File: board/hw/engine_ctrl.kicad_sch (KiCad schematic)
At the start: 6 parts, among them J3 eng, U5 DRV8220

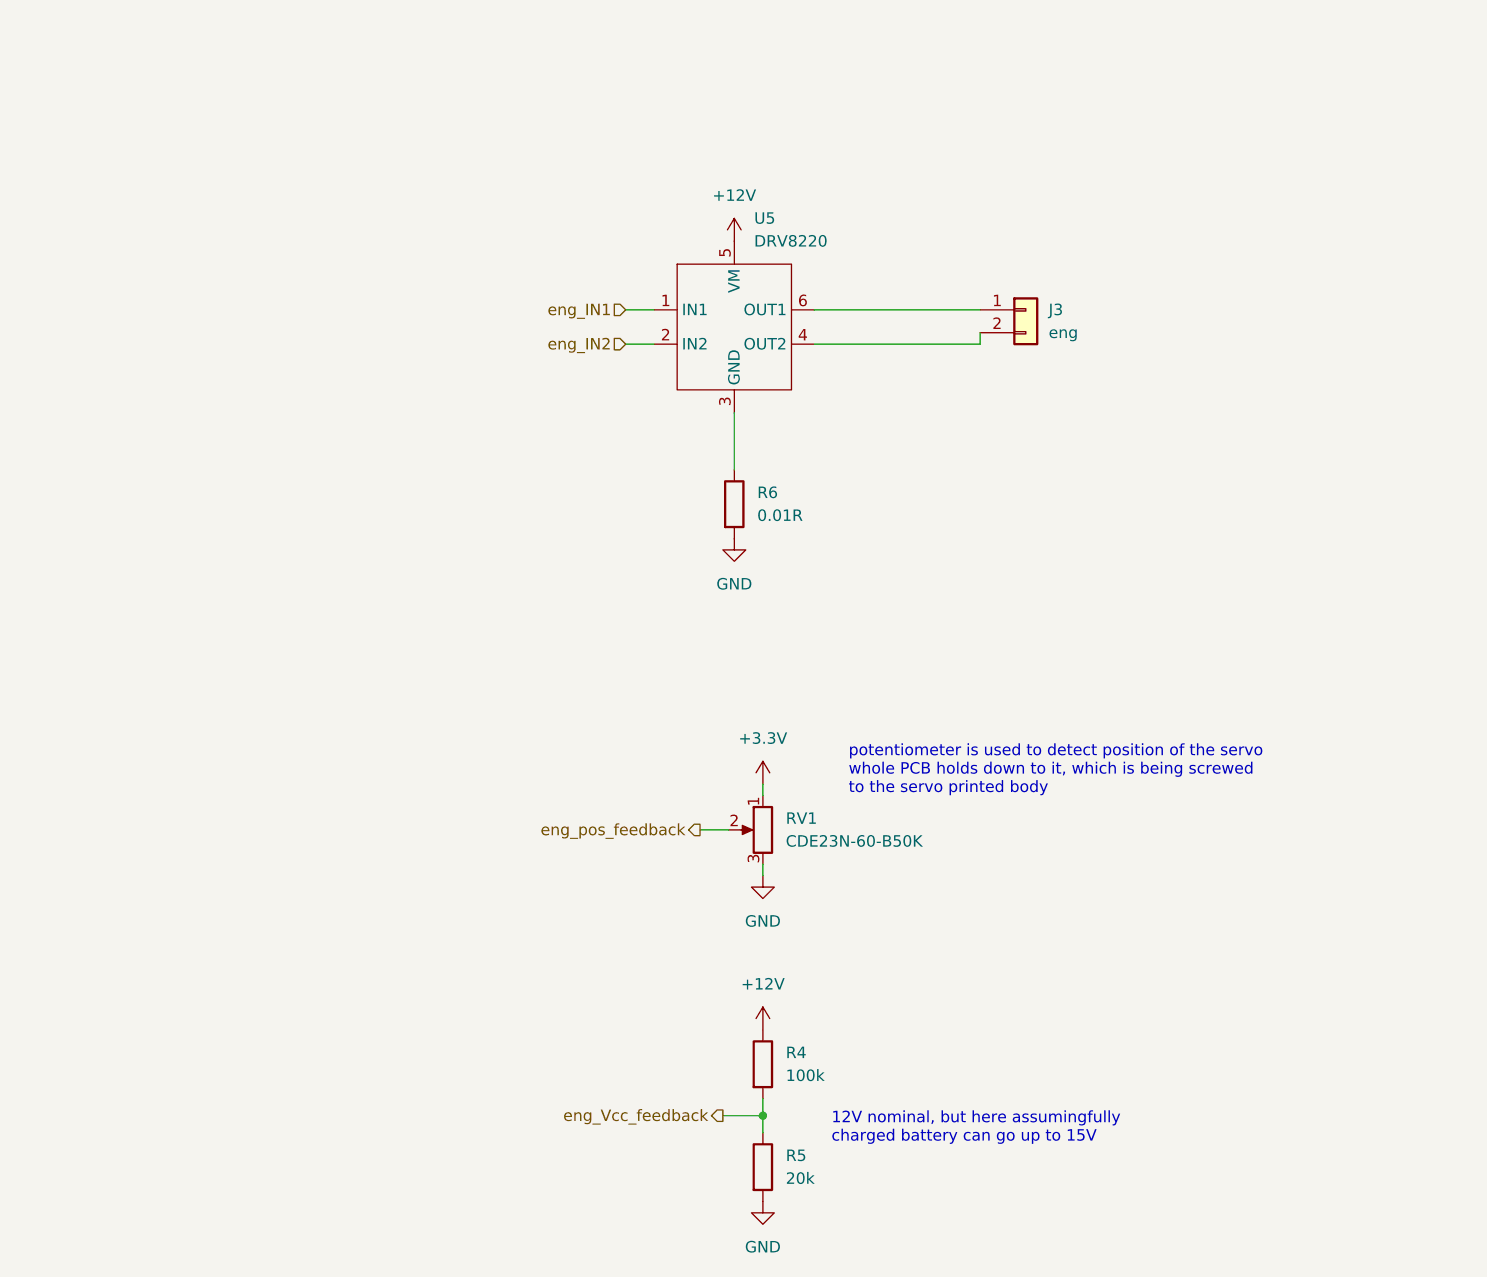
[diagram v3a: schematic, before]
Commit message: added current measuing circuit
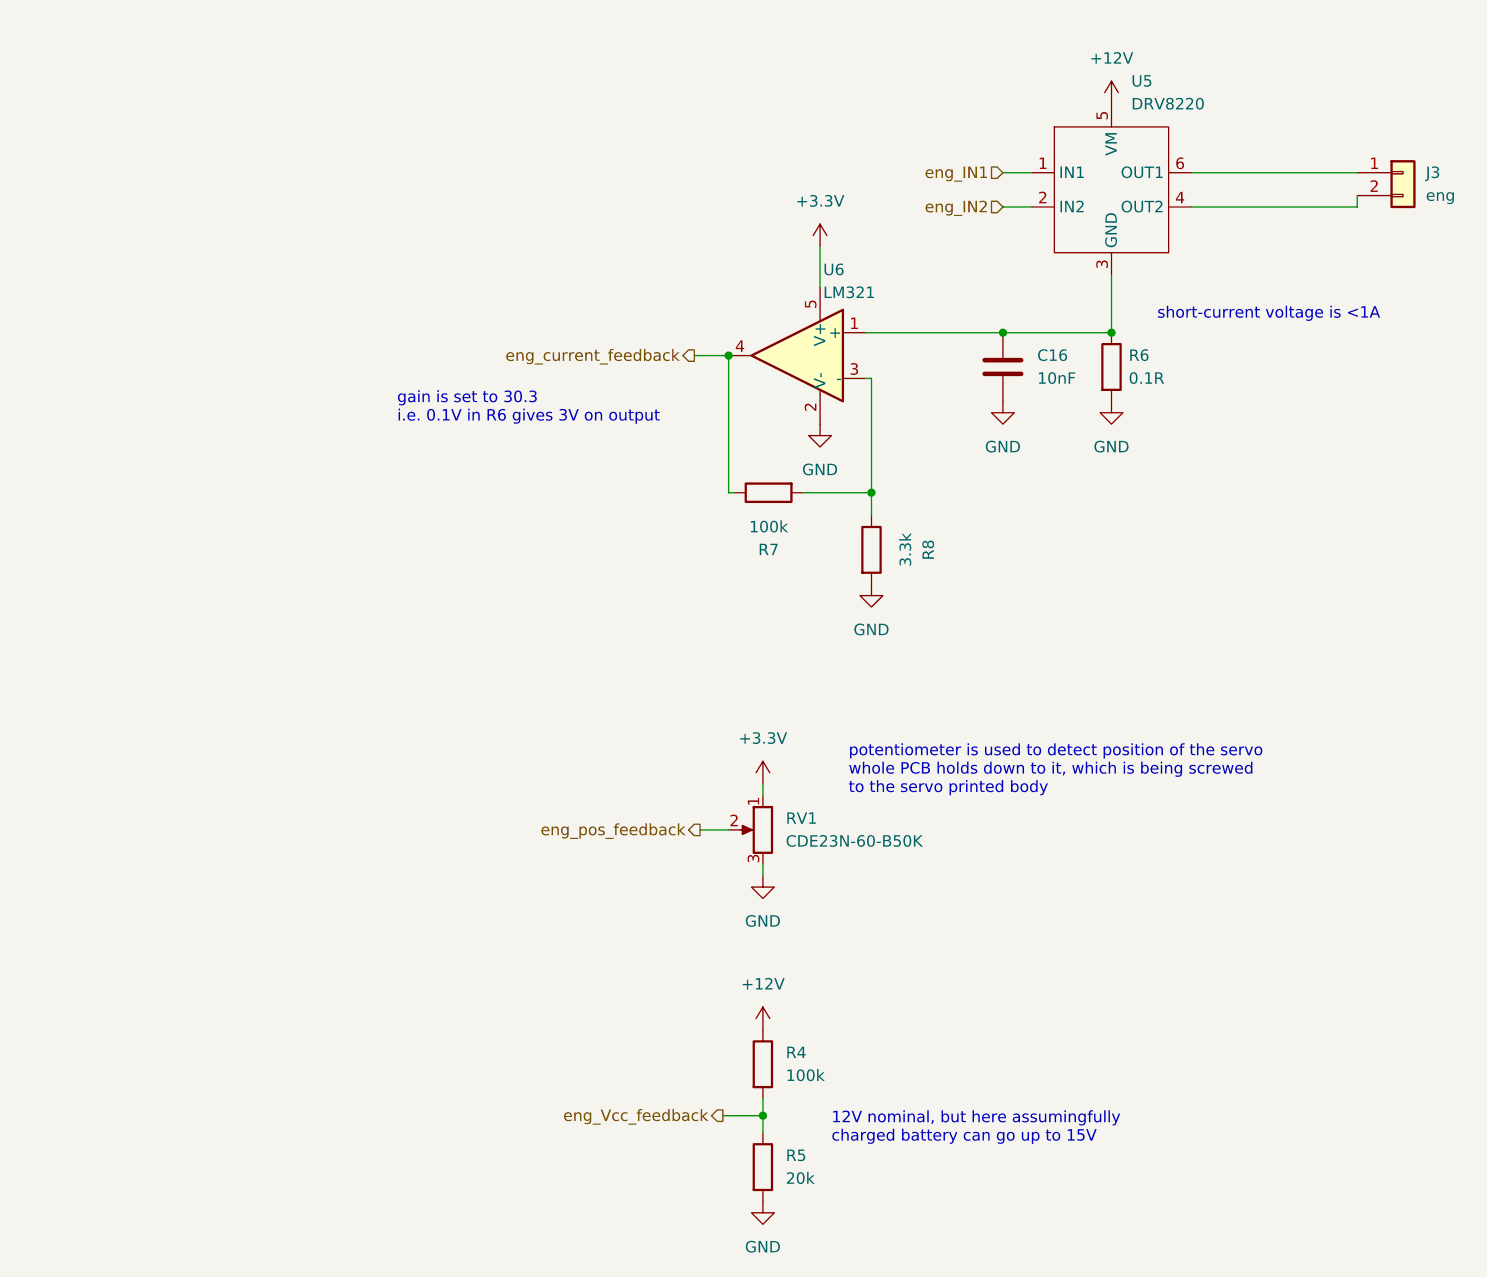
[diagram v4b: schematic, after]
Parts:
- added C16: 10nF, Capacitor_SMD:C_1206_3216Metric, symbol Device:C
- added R7: 100k, Resistor_SMD:R_0603_1608Metric, symbol Device:R
- added R8: 3.3k, Resistor_SMD:R_0603_1608Metric, symbol Device:R
- added U6: LM321, Package_TO_SOT_SMD:SOT-23-5, symbol Amplifier_Operational:LM321
- R6: value 0.01R -> 0.1R
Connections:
- net +3.3V: now also U6.5 (V+)
- net GND: now also C16.2, R8.2, U6.2 (V-)
- net at R6.1, U5.3 (GND): now also C16.1, U6.1 (+)
- new net: R7.2, R8.1, U6.3 (-)
- new net eng_current_feedback: R7.1, U6.4
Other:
- note added: "gain is set to 30.3 i.e. 0.1V in R6 gives 3V on output"
- note added: "short-current voltage is <1A"
- moved on the sheet: J3, R6, U5

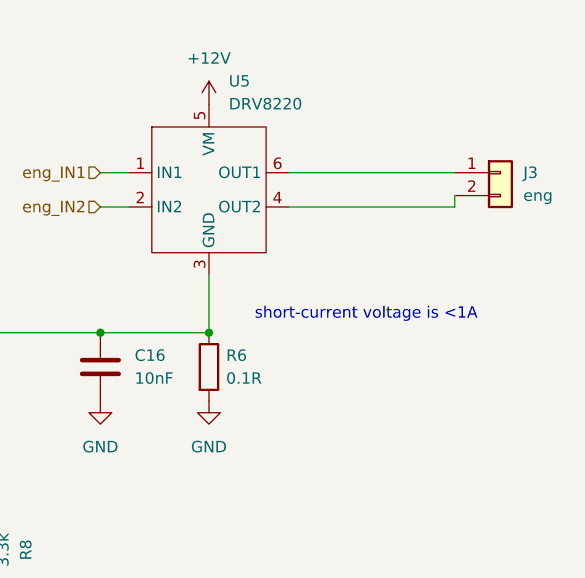
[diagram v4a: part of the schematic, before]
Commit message: engine ctrl and feedback loop elements placed
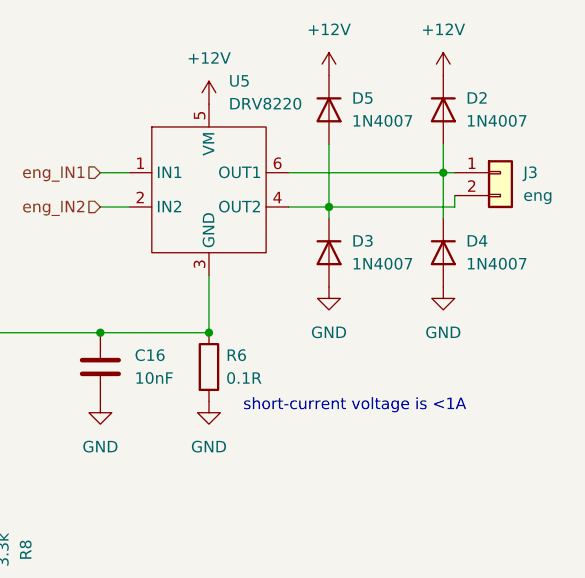
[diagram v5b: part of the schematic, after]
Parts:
- added D2, D3, D4, D5: 1N4007, Diode_SMD:D_SOD-123F, symbol Diode:1N4007
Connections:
- net +12V: now also D2.1 (K), D5.1 (K)
- net GND: now also D3.2 (A), D4.2 (A)
- net at J3.2 (Pin_2), U5.4 (OUT2): now also D3.1 (K), D5.2 (A)
- net at J3.1 (Pin_1), U5.6 (OUT1): now also D2.2 (A), D4.1 (K)
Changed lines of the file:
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@@
   (junction (at 135.89 88.9) (diameter 0) (color 0 0 0 0)
   )
+  (junction (at 161.29 74.93) (diameter 0) (color 0 0 0 0)
+  )
+  (junction (at 173.99 71.12) (diameter 0) (color 0 0 0 0)
+  )
   (junction (at 109.22 175.895) (diameter 0) (color 0 0 0 0)
   )
@@
     (stroke (width 0) (type default))
   )
+  (wire (pts (xy 161.29 76.2) (xy 161.29 74.93))
+    (stroke (width 0) (type default))
+  )
+  (wire (pts (xy 156.845 71.12) (xy 173.99 71.12))
+    (stroke (width 0) (type default))
+  )
   (wire (pts (xy 121.285 93.98) (xy 121.285 106.68))
     (stroke (width 0) (type default))
   )
-  (wire (pts (xy 156.845 74.93) (xy 175.26 74.93))
+  (wire (pts (xy 156.845 74.93) (xy 161.29 74.93))
     (stroke (width 0) (type default))
   )
@@
     (stroke (width 0) (type default))
   )
+  (wire (pts (xy 173.99 71.12) (xy 173.99 76.2))
+    (stroke (width 0) (type default))
+  )
   (wire (pts (xy 109.22 175.895) (xy 109.22 177.8))
     (stroke (width 0) (type default))
@@
     (stroke (width 0) (type default))
   )
-  (wire (pts (xy 175.26 71.12) (xy 156.845 71.12))
+  (wire (pts (xy 175.26 71.12) (xy 173.99 71.12))
     (stroke (width 0) (type default))
   )
@@
     (stroke (width 0) (type default))
   )
-  (text "short-current voltage is <1A" (at 153.035 87.63 0)
+  (wire (pts (xy 161.29 67.945) (xy 161.29 74.93))
+    (stroke (width 0) (type default))
+  )
+  (wire (pts (xy 161.29 74.93) (xy 175.26 74.93))
+    (stroke (width 0) (type default))
+  )
+  (wire (pts (xy 173.99 67.945) (xy 173.99 71.12))
+    (stroke (width 0) (type default))
+  )
+  (text "short-current voltage is <1A" (at 151.765 97.79 0)
     (effects (font (size 1.27 1.27)) (justify left bottom))
   )
@@
     )
   )
+  (symbol (lib_id "power:+12V") (at 173.99 60.325 0) (unit 1)
+    (in_bom yes) (on_board yes) (dnp no) (fields_autoplaced)
+    (property "Reference" "#PWR049" (at 173.99 64.135 0)
+      (effects (font (size 1.27 1.27)) hide)
+    )
+    (property "Value" "+12V" (at 173.99 55.245 0)
+      (effects (font (size 1.27 1.27)))
+    )
+    (property "Footprint" "" (at 173.99 60.325 0)
+      (effects (font (size 1.27 1.27)) hide)
+    )
+    (property "Datasheet" "" (at 173.99 60.325 0)
+      (effects (font (size 1.27 1.27)) hide)
+    )
+    (pin "1")
+    (instances
+      (project "yals"
+        (path "/920838ab-42d6-4f6a-a4ed-bf4606dd42d5/e7d03af2-c113-440c-81a4-7c3f8aeef75a"
+          (reference "#PWR049") (unit 1)
+        )
+      )
+    )
+  )
   (symbol (lib_id "Device:C") (at 135.89 92.71 0) (unit 1)
     (in_bom yes) (on_board yes) (dnp no) (fields_autoplaced)
@@
     )
   )
+  (symbol (lib_id "power:GND") (at 173.99 83.82 0) (mirror y) (unit 1)
+    (in_bom yes) (on_board yes) (dnp no) (fields_autoplaced)
+    (property "Reference" "#PWR047" (at 173.99 90.17 0)
+      (effects (font (size 1.27 1.27)) hide)
+    )
+    (property "Value" "GND" (at 173.99 88.9 0)
+      (effects (font (size 1.27 1.27)))
+    )
+    (property "Footprint" "" (at 173.99 83.82 0)
+      (effects (font (size 1.27 1.27)) hide)
+    )
+    (property "Datasheet" "" (at 173.99 83.82 0)
+      (effects (font (size 1.27 1.27)) hide)
+    )
+    (pin "1")
+    (instances
+      (project "yals"
+        (path "/920838ab-42d6-4f6a-a4ed-bf4606dd42d5/e7d03af2-c113-440c-81a4-7c3f8aeef75a"
+          (reference "#PWR047") (unit 1)
+        )
+      )
+    )
+  )
+  (symbol (lib_id "Diode:1N4007") (at 173.99 64.135 270) (unit 1)
+    (in_bom yes) (on_board yes) (dnp no) (fields_autoplaced)
+    (property "Reference" "D2" (at 176.53 62.865 90)
+      (effects (font (size 1.27 1.27)) (justify left))
+    )
+    (property "Value" "1N4007" (at 176.53 65.405 90)
+      (effects (font (size 1.27 1.27)) (justify left))
+    )
+    (property "Footprint" "Diode_SMD:D_SOD-123F" (at 169.545 64.135 0)
+      (effects (font (size 1.27 1.27)) hide)
+    )
+    (property "Datasheet" "http://www.vishay.com/docs/88503/1n4001.pdf" (at 173.99 64.135 0)
+      (effects (font (size 1.27 1.27)) hide)
+    )
+    (property "Sim.Device" "D" (at 173.99 64.135 0)
+      (effects (font (size 1.27 1.27)) hide)
+    )
+    (property "Sim.Pins" "1=K 2=A" (at 173.99 64.135 0)
+      (effects (font (size 1.27 1.27)) hide)
+    )
+    (pin "1")
+    (pin "2")
+    (instances
+      (project "yals"
+        (path "/920838ab-42d6-4f6a-a4ed-bf4606dd42d5/e7d03af2-c113-440c-81a4-7c3f8aeef75a"
+          (reference "D2") (unit 1)
+        )
+      )
+    )
+  )
   (symbol (lib_id "power:GND") (at 109.22 185.42 0) (unit 1)
     (in_bom yes) (on_board yes) (dnp no) (fields_autoplaced)
@@
         (path "/920838ab-42d6-4f6a-a4ed-bf4606dd42d5/e7d03af2-c113-440c-81a4-7c3f8aeef75a"
           (reference "U5") (unit 1)
+        )
+      )
+    )
+  )
+  (symbol (lib_id "power:GND") (at 161.29 83.82 0) (mirror y) (unit 1)
+    (in_bom yes) (on_board yes) (dnp no) (fields_autoplaced)
+    (property "Reference" "#PWR046" (at 161.29 90.17 0)
+      (effects (font (size 1.27 1.27)) hide)
+    )
+    (property "Value" "GND" (at 161.29 88.9 0)
+      (effects (font (size 1.27 1.27)))
+    )
+    (property "Footprint" "" (at 161.29 83.82 0)
+      (effects (font (size 1.27 1.27)) hide)
+    )
+    (property "Datasheet" "" (at 161.29 83.82 0)
+      (effects (font (size 1.27 1.27)) hide)
+    )
+    (pin "1")
+    (instances
+      (project "yals"
+        (path "/920838ab-42d6-4f6a-a4ed-bf4606dd42d5/e7d03af2-c113-440c-81a4-7c3f8aeef75a"
+          (reference "#PWR046") (unit 1)
         )
       )
@@
     )
   )
+  (symbol (lib_id "power:+12V") (at 161.29 60.325 0) (unit 1)
+    (in_bom yes) (on_board yes) (dnp no) (fields_autoplaced)
+    (property "Reference" "#PWR048" (at 161.29 64.135 0)
+      (effects (font (size 1.27 1.27)) hide)
+    )
+    (property "Value" "+12V" (at 161.29 55.245 0)
+      (effects (font (size 1.27 1.27)))
+    )
+    (property "Footprint" "" (at 161.29 60.325 0)
+      (effects (font (size 1.27 1.27)) hide)
+    )
+    (property "Datasheet" "" (at 161.29 60.325 0)
+      (effects (font (size 1.27 1.27)) hide)
+    )
+    (pin "1")
+    (instances
+      (project "yals"
+        (path "/920838ab-42d6-4f6a-a4ed-bf4606dd42d5/e7d03af2-c113-440c-81a4-7c3f8aeef75a"
+          (reference "#PWR048") (unit 1)
+        )
+      )
+    )
+  )
   (symbol (lib_id "Amplifier_Operational:LM321") (at 113.03 91.44 0) (mirror y) (unit 1)
     (in_bom yes) (on_board yes) (dnp no) (fields_autoplaced)
@@
     )
   )
+  (symbol (lib_id "Diode:1N4007") (at 173.99 80.01 270) (unit 1)
+    (in_bom yes) (on_board yes) (dnp no) (fields_autoplaced)
+    (property "Reference" "D4" (at 176.53 78.74 90)
+      (effects (font (size 1.27 1.27)) (justify left))
+    )
+    (property "Value" "1N4007" (at 176.53 81.28 90)
+      (effects (font (size 1.27 1.27)) (justify left))
+    )
+    (property "Footprint" "Diode_SMD:D_SOD-123F" (at 169.545 80.01 0)
+      (effects (font (size 1.27 1.27)) hide)
+    )
+    (property "Datasheet" "http://www.vishay.com/docs/88503/1n4001.pdf" (at 173.99 80.01 0)
+      (effects (font (size 1.27 1.27)) hide)
+    )
+    (property "Sim.Device" "D" (at 173.99 80.01 0)
+      (effects (font (size 1.27 1.27)) hide)
+    )
+    (property "Sim.Pins" "1=K 2=A" (at 173.99 80.01 0)
+      (effects (font (size 1.27 1.27)) hide)
+    )
+    (pin "1")
+    (pin "2")
+    (instances
+      (project "yals"
+        (path "/920838ab-42d6-4f6a-a4ed-bf4606dd42d5/e7d03af2-c113-440c-81a4-7c3f8aeef75a"
+          (reference "D4") (unit 1)
+        )
+      )
+    )
+  )
   (symbol (lib_id "Device:R") (at 109.22 170.18 0) (unit 1)
     (in_bom yes) (on_board yes) (dnp no) (fields_autoplaced)
@@
         )
       )
+    )
+  )
+  (symbol (lib_id "Diode:1N4007") (at 161.29 80.01 270) (unit 1)
+    (in_bom yes) (on_board yes) (dnp no) (fields_autoplaced)
+    (property "Reference" "D3" (at 163.83 78.74 90)
+      (effects (font (size 1.27 1.27)) (justify left))
+    )
+    (property "Value" "1N4007" (at 163.83 81.28 90)
+      (effects (font (size 1.27 1.27)) (justify left))
+    )
+    (property "Footprint" "Diode_SMD:D_SOD-123F" (at 156.845 80.01 0)
+      (effects (font (size 1.27 1.27)) hide)
+    )
+    (property "Datasheet" "http://www.vishay.com/docs/88503/1n4001.pdf" (at 161.29 80.01 0)
+      (effects (font (size 1.27 1.27)) hide)
+    )
+    (property "Sim.Device" "D" (at 161.29 80.01 0)
+      (effects (font (size 1.27 1.27)) hide)
+    )
+    (property "Sim.Pins" "1=K 2=A" (at 161.29 80.01 0)
+      (effects (font (size 1.27 1.27)) hide)
+    )
+    (pin "1")
+    (pin "2")
+    (instances
+      (project "yals"
+        (path "/920838ab-42d6-4f6a-a4ed-bf4606dd42d5/e7d03af2-c113-440c-81a4-7c3f8aeef75a"
+          (reference "D3") (unit 1)
+        )
+      )
+    )
+  )
+  (symbol (lib_id "Diode:1N4007") (at 161.29 64.135 270) (unit 1)
+    (in_bom yes) (on_board yes) (dnp no) (fields_autoplaced)
+    (property "Reference" "D5" (at 163.83 62.865 90)
+      (effects (font (size 1.27 1.27)) (justify left))
+    )
+    (property "Value" "1N4007" (at 163.83 65.405 90)
+      (effects (font (size 1.27 1.27)) (justify left))
+    )
+    (property "Footprint" "Diode_SMD:D_SOD-123F" (at 156.845 64.135 0)
+      (effects (font (size 1.27 1.27)) hide)
+    )
+    (property "Datasheet" "http://www.vishay.com/docs/88503/1n4001.pdf" (at 161.29 64.135 0)
+      (effects (font (size 1.27 1.27)) hide)
+    )
+    (property "Sim.Device" "D" (at 161.29 64.135 0)
+      (effects (font (size 1.27 1.27)) hide)
+    )
+    (property "Sim.Pins" "1=K 2=A" (at 161.29 64.135 0)
+      (effects (font (size 1.27 1.27)) hide)
+    )
+    (pin "1")
+    (pin "2")
+    (instances
+      (project "yals"
+        (path "/920838ab-42d6-4f6a-a4ed-bf4606dd42d5/e7d03af2-c113-440c-81a4-7c3f8aeef75a"
+          (reference "D5") (unit 1)
+        )
+      )

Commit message: fixed OpAmp description wrt gain
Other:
- note added: "gain is set to 31.3 i.e. 0.1V in R6 gives 3.13V on output"
- note removed: "gain is set to 30.3 i.e. 0.1V in R6 gives 3V on output"
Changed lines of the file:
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@@
     (effects (font (size 1.27 1.27)) (justify left bottom))
   )
-  (text "gain is set to 30.3\ni.e. 0.1V in R6 gives 3V on output"
+  (text "gain is set to 31.3\ni.e. 0.1V in R6 gives 3.13V on output"
     (at 68.58 99.06 0)
     (effects (font (size 1.27 1.27)) (justify left bottom))

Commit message: 20k -> 22k
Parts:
- R5: value 20k -> 22k
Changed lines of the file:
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@@
       (effects (font (size 1.27 1.27)) (justify left))
     )
-    (property "Value" "20k" (at 111.76 182.88 0)
+    (property "Value" "22k" (at 111.76 182.88 0)
       (effects (font (size 1.27 1.27)) (justify left))
     )
